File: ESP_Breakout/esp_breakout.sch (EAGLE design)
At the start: 7 parts

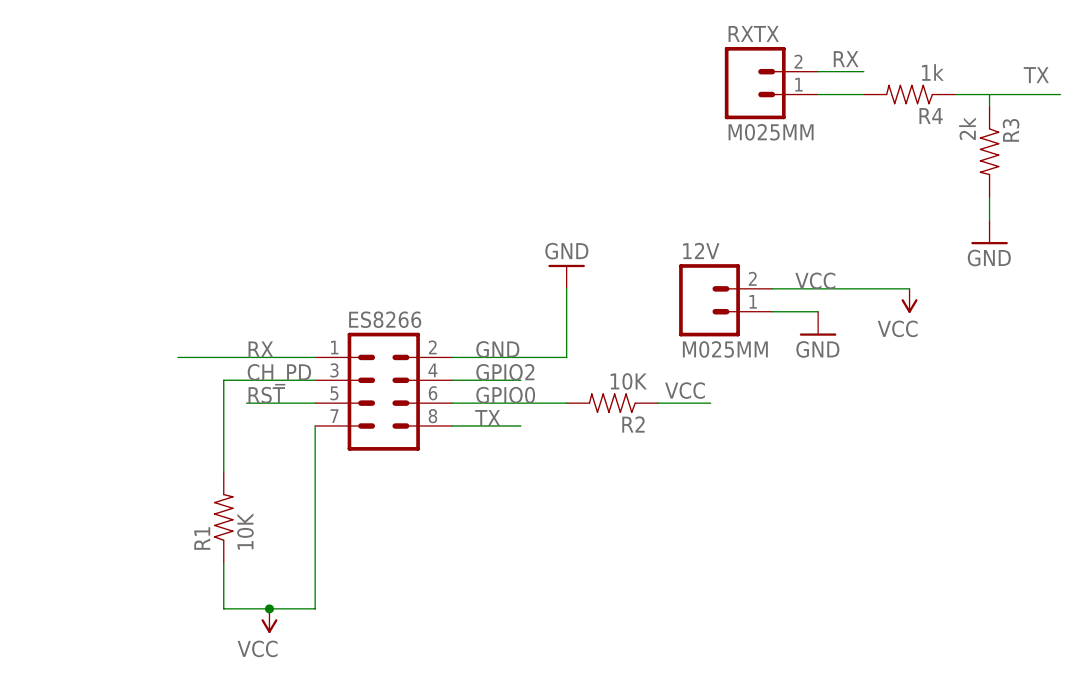
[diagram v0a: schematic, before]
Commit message: Updated ESP8266 module board for connecting to an MCU
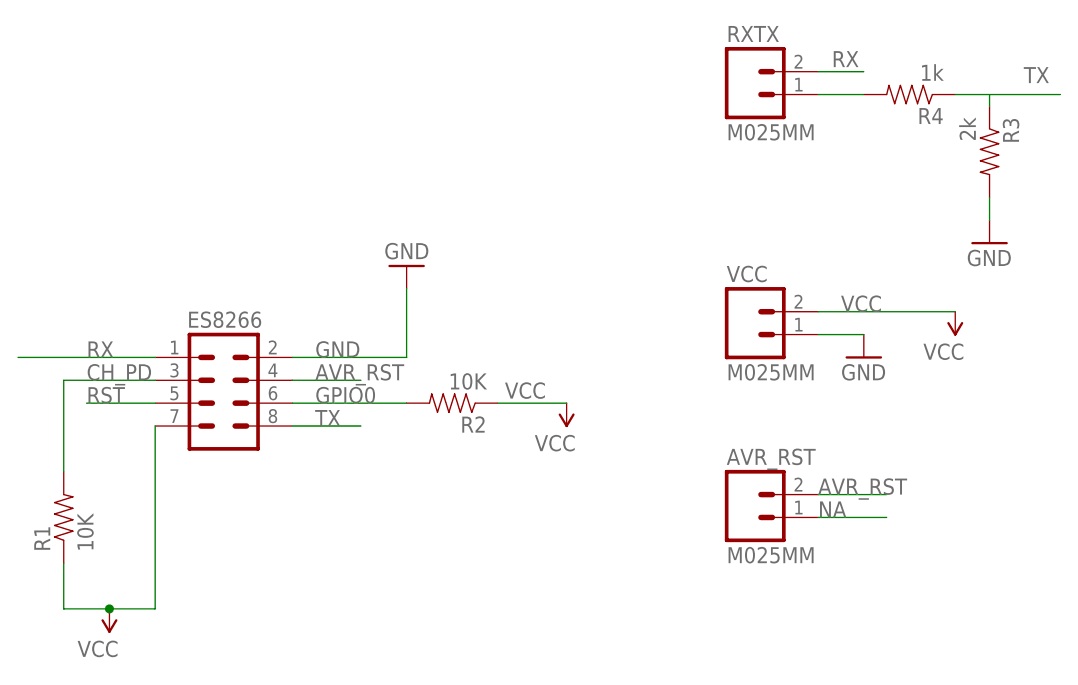
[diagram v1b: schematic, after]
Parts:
- removed 12V: M025MM, SparkFun-Connectors:M025MM
- added AVR_RST, VCC: M025MM, SparkFun-Connectors:M025MM
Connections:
- removed net GPIO2: ES8266.4
- new net AVR_RST: AVR_RST.2, ES8266.4
- new net NA: AVR_RST.1
- net GND: now also VCC.1; no longer 12V.1
- net VCC: now also VCC.2; no longer 12V.2
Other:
- moved on the sheet: ES8266, R1, R2
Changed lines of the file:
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@@
 <part name="R2" library="SparkFun-Resistors" deviceset="1KOHM-1/4W-1%(PTH)" device="" value="10K"/>
 <part name="RXTX" library="SparkFun-Connectors" deviceset="M02" device="5MM"/>
-<part name="12V" library="SparkFun-Connectors" deviceset="M02" device="5MM"/>
+<part name="VCC" library="SparkFun-Connectors" deviceset="M02" device="5MM"/>
 <part name="R3" library="SparkFun-Resistors" deviceset="1KOHM-1/4W-1%(PTH)" device="" value="2k"/>
 <part name="R4" library="SparkFun-Resistors" deviceset="1KOHM-1/4W-1%(PTH)" device="" value="1k"/>
@@
 <part name="GND5" library="SparkFun-Aesthetics" deviceset="GND" device=""/>
 <part name="SUPPLY1" library="SparkFun-Aesthetics" deviceset="VCC" device=""/>
+<part name="SUPPLY2" library="SparkFun-Aesthetics" deviceset="VCC" device=""/>
+<part name="AVR_RST" library="SparkFun-Connectors" deviceset="M02" device="5MM"/>
 </parts>
 <sheets>
@@
 </plain>
 <instances>
-<instance part="ES8266" gate="G$1" x="60.96" y="55.88"/>
-<instance part="R1" gate="G$1" x="43.18" y="43.18" rot="R90"/>
-<instance part="SUPPLY4" gate="G$1" x="48.26" y="33.02" rot="R180"/>
-<instance part="GND1" gate="1" x="81.28" y="71.12" rot="R180"/>
-<instance part="R2" gate="G$1" x="86.36" y="55.88" rot="R180"/>
+<instance part="ES8266" gate="G$1" x="43.18" y="55.88"/>
+<instance part="R1" gate="G$1" x="25.4" y="43.18" rot="R90"/>
+<instance part="SUPPLY4" gate="G$1" x="30.48" y="33.02" rot="R180"/>
+<instance part="GND1" gate="1" x="63.5" y="71.12" rot="R180"/>
+<instance part="R2" gate="G$1" x="68.58" y="55.88" rot="R180"/>
 <instance part="RXTX" gate="G$1" x="101.6" y="90.17"/>
-<instance part="12V" gate="G$1" x="96.52" y="66.04"/>
+<instance part="VCC" gate="G$1" x="101.6" y="63.5"/>
 <instance part="R3" gate="G$1" x="128.27" y="83.82" rot="R270"/>
 <instance part="R4" gate="G$1" x="119.38" y="90.17" rot="R180"/>
 <instance part="GND3" gate="1" x="128.27" y="73.66"/>
-<instance part="GND5" gate="1" x="109.22" y="63.5"/>
-<instance part="SUPPLY1" gate="G$1" x="119.38" y="68.58" rot="R180"/>
+<instance part="GND5" gate="1" x="114.3" y="60.96"/>
+<instance part="SUPPLY1" gate="G$1" x="124.46" y="66.04" rot="R180"/>
+<instance part="SUPPLY2" gate="G$1" x="81.28" y="55.88" rot="R180"/>
+<instance part="AVR_RST" gate="G$1" x="101.6" y="43.18"/>
 </instances>
 <busses>
@@
 <segment>
 <pinref part="ES8266" gate="G$1" pin="2"/>
-<wire x1="68.58" y1="60.96" x2="81.28" y2="60.96" width="0.1524" layer="91"/>
-<label x="71.12" y="60.96" size="1.778" layer="95"/>
+<wire x1="50.8" y1="60.96" x2="63.5" y2="60.96" width="0.1524" layer="91"/>
+<label x="53.34" y="60.96" size="1.778" layer="95"/>
 <pinref part="GND1" gate="1" pin="GND"/>
-<wire x1="81.28" y1="68.58" x2="81.28" y2="60.96" width="0.1524" layer="91"/>
+<wire x1="63.5" y1="68.58" x2="63.5" y2="60.96" width="0.1524" layer="91"/>
 </segment>
 <segment>
-<pinref part="12V" gate="G$1" pin="1"/>
-<wire x1="104.14" y1="66.04" x2="109.22" y2="66.04" width="0.1524" layer="91"/>
+<pinref part="VCC" gate="G$1" pin="1"/>
+<wire x1="109.22" y1="63.5" x2="114.3" y2="63.5" width="0.1524" layer="91"/>
 <pinref part="GND5" gate="1" pin="GND"/>
 </segment>
@@
 <pinref part="R1" gate="G$1" pin="1"/>
 <pinref part="SUPPLY4" gate="G$1" pin="VCC"/>
-<wire x1="43.18" y1="38.1" x2="43.18" y2="33.02" width="0.1524" layer="91"/>
-<wire x1="43.18" y1="33.02" x2="48.26" y2="33.02" width="0.1524" layer="91"/>
+<wire x1="25.4" y1="38.1" x2="25.4" y2="33.02" width="0.1524" layer="91"/>
+<wire x1="25.4" y1="33.02" x2="30.48" y2="33.02" width="0.1524" layer="91"/>
 <pinref part="ES8266" gate="G$1" pin="7"/>
-<wire x1="48.26" y1="33.02" x2="53.34" y2="33.02" width="0.1524" layer="91"/>
-<wire x1="53.34" y1="33.02" x2="53.34" y2="53.34" width="0.1524" layer="91"/>
-<junction x="48.26" y="33.02"/>
+<wire x1="30.48" y1="33.02" x2="35.56" y2="33.02" width="0.1524" layer="91"/>
+<wire x1="35.56" y1="33.02" x2="35.56" y2="53.34" width="0.1524" layer="91"/>
+<junction x="30.48" y="33.02"/>
 </segment>
 <segment>
 <pinref part="R2" gate="G$1" pin="1"/>
-<wire x1="91.44" y1="55.88" x2="97.282" y2="55.88" width="0.1524" layer="91"/>
-<label x="92.202" y="56.388" size="1.778" layer="95"/>
+<wire x1="73.66" y1="55.88" x2="81.28" y2="55.88" width="0.1524" layer="91"/>
+<label x="74.422" y="56.388" size="1.778" layer="95"/>
+<pinref part="SUPPLY2" gate="G$1" pin="VCC"/>
 </segment>
 <segment>
-<pinref part="12V" gate="G$1" pin="2"/>
-<label x="106.68" y="68.58" size="1.778" layer="95"/>
-<wire x1="104.14" y1="68.58" x2="119.38" y2="68.58" width="0.1524" layer="91"/>
+<pinref part="VCC" gate="G$1" pin="2"/>
+<label x="111.76" y="66.04" size="1.778" layer="95"/>
+<wire x1="109.22" y1="66.04" x2="124.46" y2="66.04" width="0.1524" layer="91"/>
 <pinref part="SUPPLY1" gate="G$1" pin="VCC"/>
 </segment>
@@
 <segment>
 <pinref part="ES8266" gate="G$1" pin="8"/>
-<wire x1="68.58" y1="53.34" x2="76.2" y2="53.34" width="0.1524" layer="91"/>
-<label x="71.12" y="53.34" size="1.778" layer="95"/>
+<wire x1="50.8" y1="53.34" x2="58.42" y2="53.34" width="0.1524" layer="91"/>
+<label x="53.34" y="53.34" size="1.778" layer="95"/>
 </segment>
 <segment>
@@
 <segment>
 <pinref part="ES8266" gate="G$1" pin="1"/>
-<label x="45.72" y="60.96" size="1.778" layer="95"/>
-<wire x1="38.1" y1="60.96" x2="53.34" y2="60.96" width="0.1524" layer="91"/>
+<label x="27.94" y="60.96" size="1.778" layer="95"/>
+<wire x1="20.32" y1="60.96" x2="35.56" y2="60.96" width="0.1524" layer="91"/>
 </segment>
 <segment>
@@
 <segment>
 <pinref part="ES8266" gate="G$1" pin="3"/>
-<wire x1="53.34" y1="58.42" x2="43.18" y2="58.42" width="0.1524" layer="91"/>
-<label x="45.72" y="58.42" size="1.778" layer="95"/>
+<wire x1="35.56" y1="58.42" x2="25.4" y2="58.42" width="0.1524" layer="91"/>
+<label x="27.94" y="58.42" size="1.778" layer="95"/>
 <pinref part="R1" gate="G$1" pin="2"/>
-<wire x1="43.18" y1="58.42" x2="43.18" y2="48.26" width="0.1524" layer="91"/>
+<wire x1="25.4" y1="58.42" x2="25.4" y2="48.26" width="0.1524" layer="91"/>
 </segment>
 </net>
@@
 <segment>
 <pinref part="ES8266" gate="G$1" pin="5"/>
-<wire x1="53.34" y1="55.88" x2="45.72" y2="55.88" width="0.1524" layer="91"/>
-<label x="45.72" y="55.88" size="1.778" layer="95"/>
+<wire x1="35.56" y1="55.88" x2="27.94" y2="55.88" width="0.1524" layer="91"/>
+<label x="27.94" y="55.88" size="1.778" layer="95"/>
 </segment>
 </net>
-<net name="GPIO2" class="0">
+<net name="AVR_RST" class="0">
 <segment>
 <pinref part="ES8266" gate="G$1" pin="4"/>
-<wire x1="68.58" y1="58.42" x2="76.2" y2="58.42" width="0.1524" layer="91"/>
-<label x="71.12" y="58.42" size="1.778" layer="95"/>
+<wire x1="50.8" y1="58.42" x2="58.42" y2="58.42" width="0.1524" layer="91"/>
+<label x="53.34" y="58.42" size="1.778" layer="95"/>
+</segment>
+<segment>
+<pinref part="AVR_RST" gate="G$1" pin="2"/>
+<wire x1="109.22" y1="45.72" x2="116.84" y2="45.72" width="0.1524" layer="91"/>
+<label x="109.22" y="45.72" size="1.778" layer="95"/>
 </segment>
 </net>
@@
 <segment>
 <pinref part="ES8266" gate="G$1" pin="6"/>
-<wire x1="68.58" y1="55.88" x2="81.28" y2="55.88" width="0.1524" layer="91"/>
-<label x="71.12" y="55.88" size="1.778" layer="95"/>
+<wire x1="50.8" y1="55.88" x2="63.5" y2="55.88" width="0.1524" layer="91"/>
+<label x="53.34" y="55.88" size="1.778" layer="95"/>
 <pinref part="R2" gate="G$1" pin="2"/>
 </segment>
@@
 </segment>
 </net>
+<net name="NA" class="0">
+<segment>
+<pinref part="AVR_RST" gate="G$1" pin="1"/>
+<wire x1="109.22" y1="43.18" x2="116.84" y2="43.18" width="0.1524" layer="91"/>
+<label x="109.22" y="43.18" size="1.778" layer="95"/>
+</segment>
+</net>
